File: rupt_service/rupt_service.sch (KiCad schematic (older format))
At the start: 1 part, among them P1 DIN_41612_128P

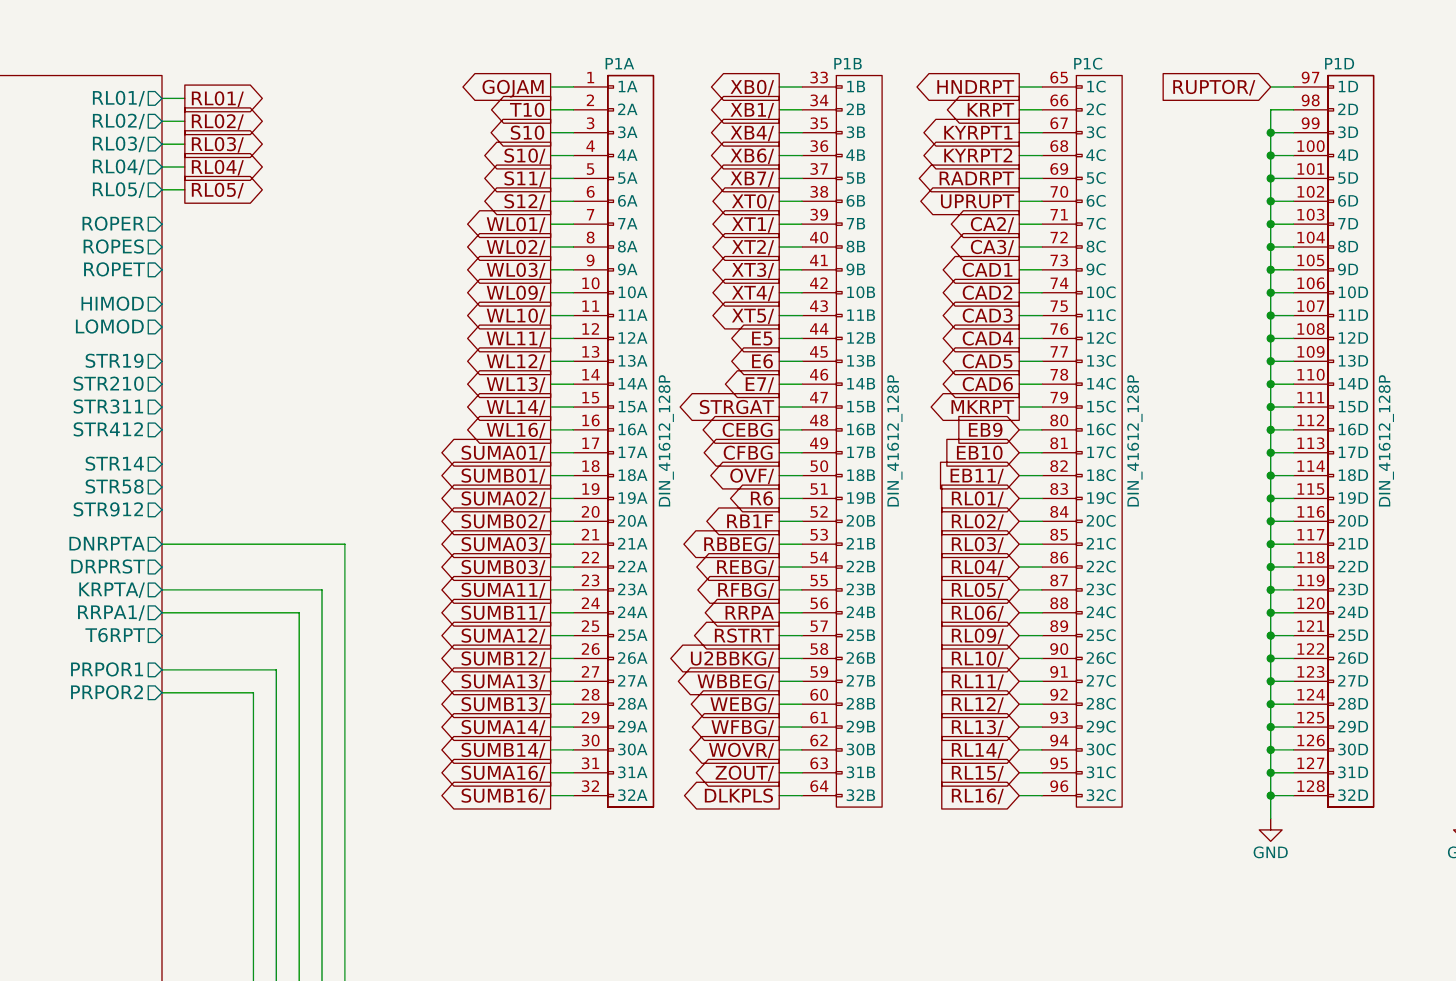
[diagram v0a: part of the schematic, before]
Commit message: New module: custom memory! This uses a flash chip and decodes address based entirely off of rope control signals.
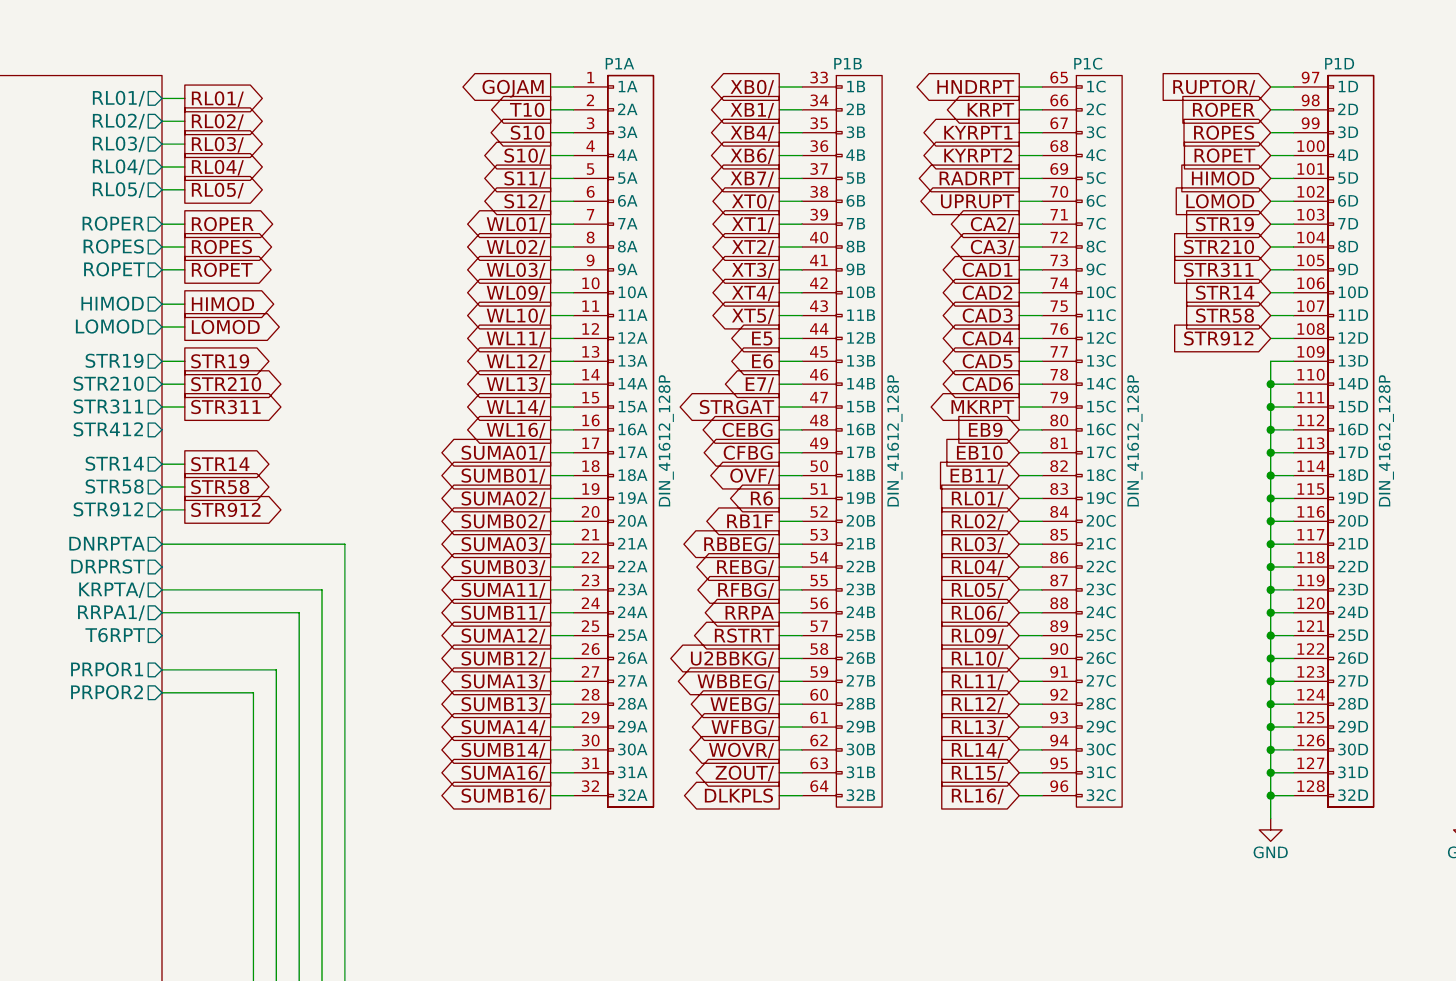
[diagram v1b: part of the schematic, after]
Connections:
- net GND: no longer P1.100 (4D), P1.101 (5D), P1.102 (6D), P1.103 (7D), P1.104 (8D), P1.105 (9D), P1.106 (10D), P1.107 (11D), P1.108 (12D), P1.98 (2D), P1.99 (3D)
- new net HIMOD: P1.101 (5D)
- new net LOMOD: P1.102 (6D)
- new net ROPER: P1.98 (2D)
- new net ROPES: P1.99 (3D)
- new net ROPET: P1.100 (4D)
- new net STR14: P1.106 (10D)
- new net STR19: P1.103 (7D)
- new net STR210: P1.104 (8D)
- new net STR311: P1.105 (9D)
- new net STR58: P1.107 (11D)
- new net STR912: P1.108 (12D)
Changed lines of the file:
@@
 $EndComp
-Wire Wire Line
-	12250 1500 12150 1500
-Wire Wire Line
-	12150 1600 12250 1600
-Connection ~ 12150 1600
-Wire Wire Line
-	12150 1700 12250 1700
-Connection ~ 12150 1700
-Wire Wire Line
-	12150 1800 12250 1800
-Connection ~ 12150 1800
-Wire Wire Line
-	12150 1900 12250 1900
-Connection ~ 12150 1900
-Wire Wire Line
-	12150 2000 12250 2000
-Connection ~ 12150 2000
-Wire Wire Line
-	12150 2100 12250 2100
-Connection ~ 12150 2100
-Wire Wire Line
-	12150 2200 12250 2200
-Connection ~ 12150 2200
-Wire Wire Line
-	12150 2300 12250 2300
-Connection ~ 12150 2300
-Wire Wire Line
-	12150 2400 12250 2400
-Connection ~ 12150 2400
-Wire Wire Line
-	12150 2500 12250 2500
-Connection ~ 12150 2500
-Wire Wire Line
-	12150 2600 12250 2600
-Connection ~ 12150 2600
-Wire Wire Line
-	12150 2700 12250 2700
-Connection ~ 12150 2700
-Wire Wire Line
-	12150 2800 12250 2800
-Connection ~ 12150 2800
 Wire Wire Line
 	12150 2900 12250 2900
@@
 RL16/
 Wire Wire Line
-	12150 1500 12150 4600
+	7300 2000 7400 2000
+Text GLabel 7400 2000 2    60   Output ~ 0
+ROPER
+Wire Wire Line
+	7300 2100 7400 2100
+Text GLabel 7400 2100 2    60   Output ~ 0
+ROPES
+Wire Wire Line
+	7300 2200 7400 2200
+Text GLabel 7400 2200 2    60   Output ~ 0
+ROPET
+Wire Wire Line
+	12250 1500 12150 1500
+Text GLabel 12150 1500 0    60   Input ~ 0
+ROPER
+Wire Wire Line
+	12250 1600 12150 1600
+Text GLabel 12150 1600 0    60   Input ~ 0
+ROPES
+Wire Wire Line
+	12250 1700 12150 1700
+Text GLabel 12150 1700 0    60   Input ~ 0
+ROPET
+Wire Wire Line
+	7300 2350 7400 2350
+Text GLabel 7400 2350 2    60   Output ~ 0
+HIMOD
+Wire Wire Line
+	7300 2450 7400 2450
+Text GLabel 7400 2450 2    60   Output ~ 0
+LOMOD
+Wire Wire Line
+	12250 1800 12150 1800
+Text GLabel 12150 1800 0    60   Input ~ 0
+HIMOD
+Wire Wire Line
+	12250 1900 12150 1900
+Text GLabel 12150 1900 0    60   Input ~ 0
+LOMOD
+Wire Wire Line
+	7300 2600 7400 2600
+Text GLabel 7400 2600 2    60   Output ~ 0
+STR19
+Wire Wire Line
+	7300 2700 7400 2700
+Text GLabel 7400 2700 2    60   Output ~ 0
+STR210
+Wire Wire Line
+	7300 2800 7400 2800
+Text GLabel 7400 2800 2    60   Output ~ 0
+STR311
+Wire Wire Line
+	12250 2000 12150 2000
+Text GLabel 12150 2000 0    60   Input ~ 0
+STR19
+Wire Wire Line
+	12250 2100 12150 2100
+Text GLabel 12150 2100 0    60   Input ~ 0
+STR210
+Wire Wire Line
+	12250 2200 12150 2200
+Text GLabel 12150 2200 0    60   Input ~ 0
+STR311
+Wire Wire Line
+	7300 3050 7400 3050
+Text GLabel 7400 3050 2    60   Output ~ 0
+STR14
+Wire Wire Line
+	7300 3150 7400 3150
+Text GLabel 7400 3150 2    60   Output ~ 0
+STR58
+Wire Wire Line
+	7300 3250 7400 3250
+Text GLabel 7400 3250 2    60   Output ~ 0
+STR912
+Wire Wire Line
+	12250 2300 12150 2300
+Text GLabel 12150 2300 0    60   Input ~ 0
+STR14
+Wire Wire Line
+	12250 2400 12150 2400
+Text GLabel 12150 2400 0    60   Input ~ 0
+STR58
+Wire Wire Line
+	12250 2500 12150 2500
+Text GLabel 12150 2500 0    60   Input ~ 0
+STR912
+Wire Wire Line
+	12150 2700 12250 2700
+Connection ~ 12150 2700
+Wire Wire Line
+	12150 2800 12250 2800
+Connection ~ 12150 2800
+Wire Wire Line
+	12250 2600 12150 2600
+Wire Wire Line
+	12150 2600 12150 4600
 $EndSCHEMATC

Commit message: Updated fixed memory model, plus various bugfixes
Rope memory control signals are now decoded much earlier in the cycle to
determine the target address, allowing slower memory devices (such as
the EPCS on the DE0 Nano) enough time to load their data.

The bugfixes are mostly wiring errors discovered by debugging lockups in
when running Colossus 237 -- all were causing the ST2 pulse to not
occur, so errors that *don't* prevent ST2 from happening very well might
be present in the instructions that have been fixed.

The computer now gets through the initialization code and enters an
infinite loop when attempting to invoke the interpeter, due to the lack
of erasable memory.
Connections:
- net GND: no longer P1.109 (13D)
- net STR14: now also P1.107 (11D); no longer P1.106 (10D)
- net STR58: now also P1.108 (12D); no longer P1.107 (11D)
- net STR912: now also P1.109 (13D); no longer P1.108 (12D)
- new net STR412: P1.106 (10D)
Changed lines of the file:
@@
 STR912
-Wire Wire Line
-	12250 2300 12150 2300
-Text GLabel 12150 2300 0    60   Input ~ 0
-STR14
 Wire Wire Line
 	12250 2400 12150 2400
 Text GLabel 12150 2400 0    60   Input ~ 0
-STR58
+STR14
 Wire Wire Line
 	12250 2500 12150 2500
 Text GLabel 12150 2500 0    60   Input ~ 0
+STR58
+Wire Wire Line
+	12250 2600 12150 2600
+Text GLabel 12150 2600 0    60   Input ~ 0
 STR912
 Wire Wire Line
 	12150 2700 12250 2700
-Connection ~ 12150 2700
 Wire Wire Line
 	12150 2800 12250 2800
 Connection ~ 12150 2800
 Wire Wire Line
-	12250 2600 12150 2600
+	7300 2900 7400 2900
+Text GLabel 7400 2900 2    60   Output ~ 0
+STR412
 Wire Wire Line
-	12150 2600 12150 4600
+	12150 2700 12150 4600
+Wire Wire Line
+	12250 2300 12150 2300
+Text GLabel 12150 2300 0    60   Input ~ 0
+STR412
 $EndSCHEMATC

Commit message: Added and tied in Inout V.
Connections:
- net GND: no longer P1.110 (14D)
- new net DRPRST: P1.110 (14D)
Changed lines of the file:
@@
 STR912
 Wire Wire Line
-	12150 2700 12250 2700
-Wire Wire Line
 	12150 2800 12250 2800
-Connection ~ 12150 2800
 Wire Wire Line
 	7300 2900 7400 2900
@@
 STR412
 Wire Wire Line
-	12150 2700 12150 4600
-Wire Wire Line
 	12250 2300 12150 2300
 Text GLabel 12150 2300 0    60   Input ~ 0
 STR412
+Wire Wire Line
+	7300 3500 7400 3500
+Text GLabel 7400 3500 2    60   Output ~ 0
+DRPRST
+Wire Wire Line
+	12150 2800 12150 4600
+Wire Wire Line
+	12250 2700 12150 2700
+Text GLabel 12150 2700 0    60   Input ~ 0
+DRPRST
 $EndSCHEMATC

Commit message: Added and tied in Inout VI. Pulled in all PIPA related things. Almost there!
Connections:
- net DRPRST: now also P1.111 (15D); no longer P1.110 (14D)
- net GND: no longer P1.111 (15D)
- new net T6RPT: P1.110 (14D)
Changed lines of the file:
@@
 Wire Wire Line
 	12150 2900 12250 2900
-Connection ~ 12150 2900
 Wire Wire Line
 	12150 3000 12250 3000
@@
 STR912
 Wire Wire Line
-	12150 2800 12250 2800
-Wire Wire Line
 	7300 2900 7400 2900
 Text GLabel 7400 2900 2    60   Output ~ 0
@@
 DRPRST
 Wire Wire Line
-	12150 2800 12150 4600
+	12250 2800 12150 2800
+Text GLabel 12150 2800 0    60   Input ~ 0
+DRPRST
+Wire Wire Line
+	7300 3800 7400 3800
+Text GLabel 7400 3800 2    60   Output ~ 0
+T6RPT
+Wire Wire Line
+	12150 2900 12150 4600
 Wire Wire Line
 	12250 2700 12150 2700
 Text GLabel 12150 2700 0    60   Input ~ 0
-DRPRST
+T6RPT
 $EndSCHEMATC

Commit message: Updated Rupt Service to be on +4VSW
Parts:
- added U15001, U15006, U15007, U15009, U15011, U15013, U15015, U15018, U15020, U15024, U15027, U15029, U15033, U15037, U15043, U15045, U15048, U15056, U15057: 74HC02, symbol 74HC02
- added U15002, U15005, U15008, U15010, U15014, U15021, U15023, U15025, U15028, U15030, U15031, U15032, U15034, U15035, U15036, U15038, U15040, U15042, U15046, U15047, U15050, U15051, U15052, U15054, U15055, U15058: 74HC27, symbol 74HC27
- added U15003, U15019, U15022, U15044, U15049, U15053, U15059: 74HC04, symbol 74HC04
- added U15004, U15016, U15039: 74LVC07, symbol 74LVC07
- added U15012, U15017, U15026, U15041: 74HC4002, symbol 74HC4002
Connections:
- net labels added: +4VSW
- net labels removed: VCC
- wire segments 383 -> 395

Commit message: This adds fixes to the schematics for changes identified in comparing against the independent AGC schematics in the "schematics" branch of the main Virtual AGC repository.  Changes include:  Topological (but not logical) fixes to the DKCTR4,5,4/,5/ signals in the inout_v schematic. Wiring fix (incorrect signal sources for 5 gates) in inout_iv. Fixed incorrect signal source (including MGOJAM output polarity) for one gate in timer.  Fixed incorrect topology (but not logic) for 3 output signals in service_gates. Fixed backplane signal source (MYCLMP incorrectly used everywhere in place of the correct STRT2) in memory_timing_addressing.  ROPER, ROPES, ROPET had incorrectly omitted STRT2 as an input signal in four_bit_2. A couple of  internal nets local to sheets were also renamed due to conflicts with analysis software.  None of these fixes had any measurable effect on instruction execution; Validation was passed prior to the fixes, and continues to be passed after the fixes, and the identical instruction sequence occurs in doing so.
For me, warnings about missing components from the libraries occur upon every schematic load, though
these missing components don't seem to actually be in the circuits.  I tried to make some library
changes to work around that.  My changes don't actually fix the problem, but rather than try to back
them out and redo all the testing, they're a part of this commit as well.
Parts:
- added U15060: 74HC02, symbol 74HC02
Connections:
- net labels added: STRT2
- wire segments 395 -> 396
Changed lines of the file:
@@
 LIBS:valves
 LIBS:rupt_service-cache
-EELAYER 25 0
+EELAYER 26 0
 EELAYER END
 $Descr A2 23386 16535
@@
 Wire Wire Line
 	12150 3000 12250 3000
-Connection ~ 12150 3000
 Wire Wire Line
 	12150 3100 12250 3100
@@
 Wire Wire Line
 	13850 1400 13850 1300
-$Sheet
-S 5950 1350 1350 5600
-U 56E5D485
-F0 "A15_2" 60
-F1 "a15_2.sch" 60
-F2 "WOVR/" I L 5950 5050 60
-F3 "OVF/" I L 5950 4650 60
-F4 "CA3/" I L 5950 6200 60
-F5 "XB1/" I L 5950 3200 60
-F6 "ZOUT/" I L 5950 5150 60
-F7 "T6RPT" O R 7300 3800 60
-F8 "GOJAM" I L 5950 1450 60
-F9 "XT0/" I L 5950 3600 60
-F10 "XB4/" I L 5950 3300 60
-F11 "KRPT" I L 5950 5400 60
-F12 "XB0/" I L 5950 3100 60
-F13 "XT1/" I L 5950 3700 60
-F14 "CA2/" I L 5950 6100 60
-F15 "XB6/" I L 5950 3400 60
-F16 "XB7/" I L 5950 3500 60
-F17 "XT2/" I L 5950 3800 60
-F18 "KYRPT1" I L 5950 5500 60
-F19 "KRPTA/" O R 7300 3600 60
-F20 "KYRPT2" I L 5950 5600 60
-F21 "MKRPT" I L 5950 6850 60
-F22 "XT3/" I L 5950 3900 60
-F23 "UPRUPT" I L 5950 5700 60
-F24 "DLKPLS" I L 5950 5300 60
-F25 "XT4/" I L 5950 4000 60
-F26 "DNRPTA" O R 7300 3400 60
-F27 "DRPRST" O R 7300 3500 60
-F28 "PRPOR1" O R 7300 3950 60
-F29 "PRPOR2" O R 7300 4050 60
-F30 "RRPA" I L 5950 4950 60
-F31 "RRPA1/" O R 7300 3700 60
-F32 "PRPOR3" I L 5950 5850 60
-F33 "PRPOR4" I L 5950 5950 60
-F34 "BBK3" I L 5950 4350 60
-F35 "CAD3" I L 5950 6500 60
-F36 "RL03/" O R 7300 1650 60
-F37 "RL04/" O R 7300 1750 60
-F38 "CAD4" I L 5950 6600 60
-F39 "RL05/" O R 7300 1850 60
-F40 "CAD5" I L 5950 6700 60
-F41 "RL02/" O R 7300 1550 60
-F42 "CAD2" I L 5950 6400 60
-F43 "BBK2" I L 5950 4250 60
-F44 "R6" I L 5950 4750 60
-F45 "RL01/" O R 7300 1450 60
-F46 "CAD1" I L 5950 6300 60
-F47 "BBK1" I L 5950 4150 60
-F48 "RB1F" I L 5950 4850 60
-F49 "STRGAT" I L 5950 4500 60
-F50 "STR412" O R 7300 2900 60
-F51 "STR311" O R 7300 2800 60
-F52 "STR210" O R 7300 2700 60
-F53 "STR19" O R 7300 2600 60
-F54 "F11" I L 5950 1850 60
-F55 "F11/" I L 5950 1950 60
-F56 "S10" I L 5950 1600 60
-F57 "S10/" I L 5950 1700 60
-F58 "F16" I L 5950 2850 60
-F59 "F15" I L 5950 2650 60
-F60 "F14/" I L 5950 2550 60
-F61 "F13/" I L 5950 2350 60
-F62 "F13" I L 5950 2250 60
-F63 "F14" I L 5950 2450 60
-F64 "F15/" I L 5950 2750 60
-F65 "F16/" I L 5950 2950 60
-F66 "F12" I L 5950 2050 60
-F67 "F12/" I L 5950 2150 60
-F68 "STR14" O R 7300 3050 60
-F69 "ROPER" O R 7300 2000 60
-F70 "LOMOD" O R 7300 2450 60
-F71 "STR58" O R 7300 3150 60
-F72 "ROPES" O R 7300 2100 60
-F73 "HIMOD" O R 7300 2350 60
-F74 "STR912" O R 7300 3250 60
-F75 "ROPET" O R 7300 2200 60
-$EndSheet
 Wire Wire Line
 	2100 1450 2000 1450
@@
 GOJAM
 Wire Wire Line
-	5950 1450 5850 1450
-Text GLabel 5850 1450 0    60   Input ~ 0
+	5950 1400 5850 1400
+Text GLabel 5850 1400 0    60   Input ~ 0
 GOJAM
 Wire Wire Line
@@
 T10
 Wire Wire Line
-	5950 1600 5850 1600
-Text GLabel 5850 1600 0    60   Input ~ 0
+	5950 1625 5850 1625
+Text GLabel 5850 1625 0    60   Input ~ 0
 S10
 Wire Wire Line
-	5950 1700 5850 1700
-Text GLabel 5850 1700 0    60   Input ~ 0
+	5950 1725 5850 1725
+Text GLabel 5850 1725 0    60   Input ~ 0
 S10/
 Wire Wire Line
@@
 Text GLabel 7400 3800 2    60   Output ~ 0
 T6RPT
-Wire Wire Line
-	12150 2900 12150 4600
 Wire Wire Line
 	12250 2700 12150 2700
@@
 	9400 5200 17000 5200
 Wire Wire Line
-	17000 5700 9400 5700
+	9400 5700 17000 5700
 Wire Wire Line
 	9400 6250 17000 6250
 Wire Wire Line
-	17000 6750 9400 6750
-Wire Wire Line
-	9600 7300 16800 7300
-Wire Wire Line
-	16800 7800 9600 7800
+	9400 6750 17000 6750
+Wire Wire Line
+	9600 7300 17200 7300
+Wire Wire Line
+	9600 7800 17200 7800
 Connection ~ 9800 5200
 Connection ~ 10200 5200
@@
 Wire Wire Line
 	13200 7800 13200 7850
+$Comp
+L 74HC02 U15060
+U 5 1 5BD617FA
+P 17200 7550
+F 0 "U15060" H 17200 7600 60  0000 C CNN
+F 1 "74HC02" H 17200 7500 60  0001 C CNN
+F 2 "" H 17200 7550 60  0000 C CNN
+F 3 "" H 17200 7550 60  0000 C CNN
+	5    17200 7550
+	1    0    0    -1
+$EndComp
+Connection ~ 16800 7300
+Connection ~ 16800 7800
+Wire Wire Line
+	12150 3000 12150 4600
+Text GLabel 12150 2900 0    60   Output ~ 0
+STRT2
+$Sheet
+S 5950 1350 1350 5600
+U 56E5D485
+F0 "A15_2" 60
+F1 "a15_2.sch" 60
+F2 "WOVR/" I L 5950 5050 60
+F3 "OVF/" I L 5950 4650 60
+F4 "CA3/" I L 5950 6200 60
+F5 "XB1/" I L 5950 3200 60
+F6 "ZOUT/" I L 5950 5150 60
+F7 "T6RPT" O R 7300 3800 60
+F8 "GOJAM" I L 5950 1400 60
+F9 "XT0/" I L 5950 3600 60
+F10 "XB4/" I L 5950 3300 60
+F11 "KRPT" I L 5950 5400 60
+F12 "XB0/" I L 5950 3100 60
+F13 "XT1/" I L 5950 3700 60
+F14 "CA2/" I L 5950 6100 60
+F15 "XB6/" I L 5950 3400 60
+F16 "XB7/" I L 5950 3500 60
+F17 "XT2/" I L 5950 3800 60
+F18 "KYRPT1" I L 5950 5500 60
+F19 "KRPTA/" O R 7300 3600 60
+F20 "KYRPT2" I L 5950 5600 60
+F21 "MKRPT" I L 5950 6850 60
+F22 "XT3/" I L 5950 3900 60
+F23 "UPRUPT" I L 5950 5700 60
+F24 "DLKPLS" I L 5950 5300 60
+F25 "XT4/" I L 5950 4000 60
+F26 "DNRPTA" O R 7300 3400 60
+F27 "DRPRST" O R 7300 3500 60
+F28 "PRPOR1" O R 7300 3950 60
+F29 "PRPOR2" O R 7300 4050 60
+F30 "RRPA" I L 5950 4950 60
+F31 "RRPA1/" O R 7300 3700 60
+F32 "PRPOR3" I L 5950 5850 60
+F33 "PRPOR4" I L 5950 5950 60
+F34 "BBK3" I L 5950 4350 60
+F35 "CAD3" I L 5950 6500 60
+F36 "RL03/" O R 7300 1650 60
+F37 "RL04/" O R 7300 1750 60
+F38 "CAD4" I L 5950 6600 60
+F39 "RL05/" O R 7300 1850 60
+F40 "CAD5" I L 5950 6700 60
+F41 "RL02/" O R 7300 1550 60
+F42 "CAD2" I L 5950 6400 60
+F43 "BBK2" I L 5950 4250 60
+F44 "R6" I L 5950 4750 60
+F45 "RL01/" O R 7300 1450 60
+F46 "CAD1" I L 5950 6300 60
+F47 "BBK1" I L 5950 4150 60
+F48 "RB1F" I L 5950 4850 60
+F49 "STRGAT" I L 5950 4500 60
+F50 "STR412" O R 7300 2900 60
+F51 "STR311" O R 7300 2800 60
+F52 "STR210" O R 7300 2700 60
+F53 "STR19" O R 7300 2600 60
+F54 "F11" I L 5950 1850 60
+F55 "F11/" I L 5950 1950 60
+F56 "S10" I L 5950 1625 60
+F57 "S10/" I L 5950 1725 60
+F58 "F16" I L 5950 2850 60
+F59 "F15" I L 5950 2650 60
+F60 "F14/" I L 5950 2550 60
+F61 "F13/" I L 5950 2350 60
+F62 "F13" I L 5950 2250 60
+F63 "F14" I L 5950 2450 60
+F64 "F15/" I L 5950 2750 60
+F65 "F16/" I L 5950 2950 60
+F66 "F12" I L 5950 2050 60
+F67 "F12/" I L 5950 2150 60
+F68 "STR14" O R 7300 3050 60
+F69 "ROPER" O R 7300 2000 60
+F70 "LOMOD" O R 7300 2450 60
+F71 "STR58" O R 7300 3150 60
+F72 "ROPES" O R 7300 2100 60
+F73 "HIMOD" O R 7300 2350 60
+F74 "STR912" O R 7300 3250 60
+F75 "ROPET" O R 7300 2200 60
+F76 "STRT2" I L 5950 1500 60
+$EndSheet
+Text GLabel 5850 1500 0    60   Input ~ 0
+STRT2
+Wire Wire Line
+	5850 1500 5950 1500
 $EndSCHEMATC
